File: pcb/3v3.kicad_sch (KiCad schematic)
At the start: 7 parts, among them U6 AP3441SHE-7B

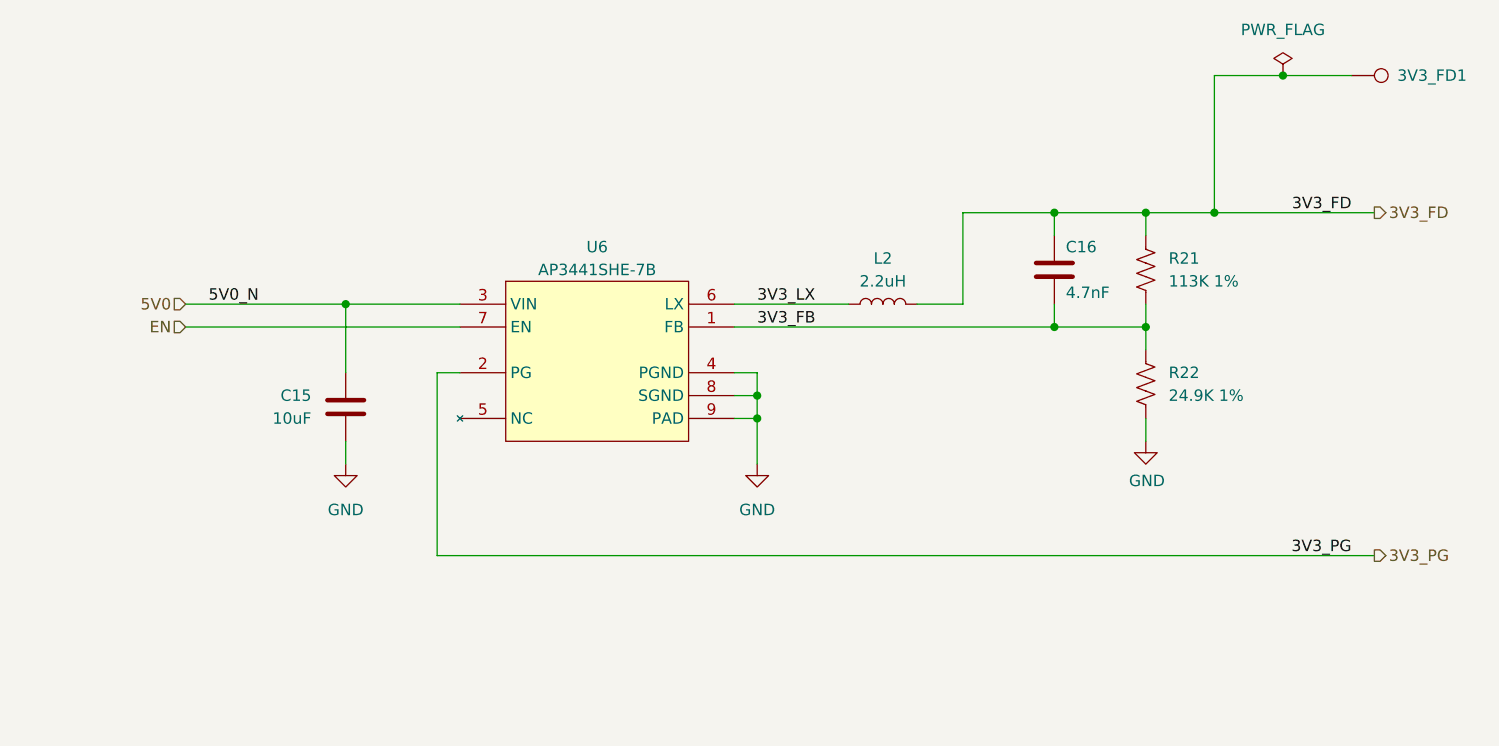
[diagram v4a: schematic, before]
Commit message: added mig ddr pinout constraints
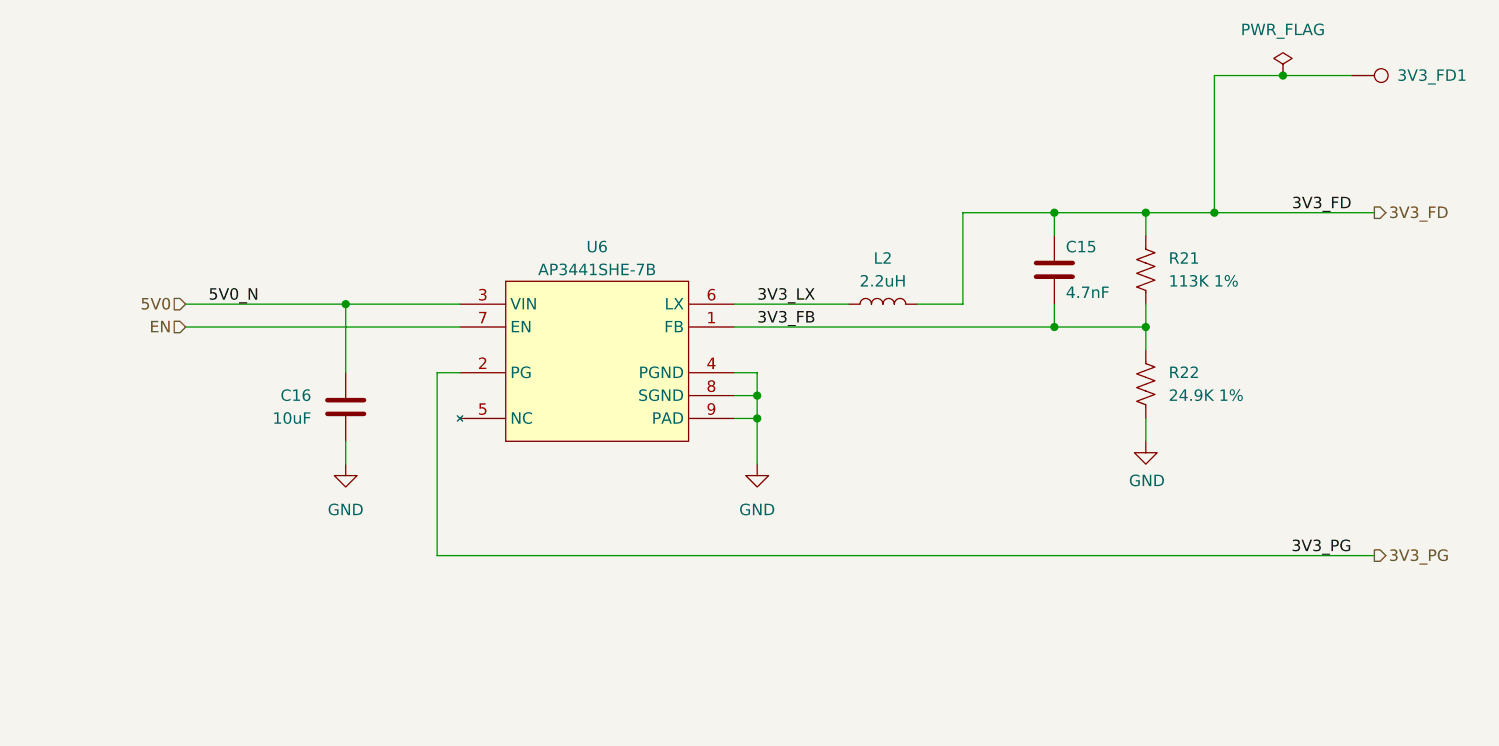
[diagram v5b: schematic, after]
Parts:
- C16: renamed from C15; footprint Capacitor_SMD:C_0402_1005Metric -> Capacitor_SMD:C_1206_3216Metric; Manufacturer Murata Electronics -> KYOCERA AVX; Manufacturer Product Number GRM155R61A106ME11D -> TAJA106M010RNJ; Part Description CAP CER 10UF 10V X5R 0402 -> CAP TANT 10UF 20% 10V 1206
- renumbered C16 to C15
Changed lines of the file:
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@@
 		(on_board yes)
 		(dnp no)
-		(property "Reference" "#PWR022"
+		(property "Reference" "#PWR020"
 			(at 182.88 110.49 0)
 			(effects
@@
 			(project "RPi-HwAB-1"
 				(path "/e63e39d7-6ac0-4ffd-8aa3-1841a4541b55/f9ebb56c-78c7-42ac-bc19-ccbf788f5318/623ac269-424c-4b40-80d6-6e60349ac538"
-					(reference "#PWR022")
+					(reference "#PWR020")
 					(unit 1)
 				)
@@
 		(dnp no)
 		(fields_autoplaced yes)
-		(property "Reference" "#PWR021"
+		(property "Reference" "#PWR022"
 			(at 139.7 113.03 0)
 			(effects
@@
 			(project "RPi-HwAB-1"
 				(path "/e63e39d7-6ac0-4ffd-8aa3-1841a4541b55/f9ebb56c-78c7-42ac-bc19-ccbf788f5318/623ac269-424c-4b40-80d6-6e60349ac538"
-					(reference "#PWR021")
+					(reference "#PWR022")
 					(unit 1)
 				)
@@
 		(dnp no)
 		(fields_autoplaced yes)
-		(property "Reference" "#PWR020"
+		(property "Reference" "#PWR021"
 			(at 93.98 113.03 0)
 			(effects
@@
 			(project "RPi-HwAB-1"
 				(path "/e63e39d7-6ac0-4ffd-8aa3-1841a4541b55/f9ebb56c-78c7-42ac-bc19-ccbf788f5318/623ac269-424c-4b40-80d6-6e60349ac538"
-					(reference "#PWR020")
+					(reference "#PWR021")
 					(unit 1)
 				)
@@
 		(on_board yes)
 		(dnp no)
-		(property "Reference" "C16"
+		(property "Reference" "C15"
 			(at 173.99 82.55 0)
 			(effects
@@
 			(project "RPi-HwAB-1"
 				(path "/e63e39d7-6ac0-4ffd-8aa3-1841a4541b55/f9ebb56c-78c7-42ac-bc19-ccbf788f5318/623ac269-424c-4b40-80d6-6e60349ac538"
-					(reference "C16")
+					(reference "C15")
 					(unit 1)
 				)
@@
 		(on_board yes)
 		(dnp no)
-		(property "Reference" "C15"
+		(property "Reference" "C16"
 			(at 90.17 99.0599 0)
 			(effects
@@
 			)
 		)
-		(property "Footprint" "Capacitor_SMD:C_0402_1005Metric"
+		(property "Footprint" "Capacitor_SMD:C_1206_3216Metric"
 			(at 94.9452 104.14 0)
 			(effects
@@
 			)
 		)
-		(property "Manufacturer" "Murata Electronics"
+		(property "Manufacturer" "KYOCERA AVX"
 			(at 93.98 100.33 0)
 			(effects
@@
 			)
 		)
-		(property "Manufacturer Product Number" "GRM155R61A106ME11D"
+		(property "Manufacturer Product Number" "TAJA106M010RNJ"
 			(at 93.98 100.33 0)
 			(effects
@@
 			)
 		)
-		(property "Part Description" "CAP CER 10UF 10V X5R 0402"
+		(property "Part Description" "CAP TANT 10UF 20% 10V 1206"
 			(at 93.98 100.33 0)
 			(effects
@@
 			(project "RPi-HwAB-1"
 				(path "/e63e39d7-6ac0-4ffd-8aa3-1841a4541b55/f9ebb56c-78c7-42ac-bc19-ccbf788f5318/623ac269-424c-4b40-80d6-6e60349ac538"
-					(reference "C15")
-					(unit 1)
-				)
+					(reference "C16")
+					(unit 1)
+				)
